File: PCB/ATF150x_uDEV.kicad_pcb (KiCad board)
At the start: 2 copper layers, 50.8 x 20.3 mm, 14 parts, among them J1 Altera JTAG-A+VPP, J2 VERT, J3 VERT, U1 ATF150x-xAx44

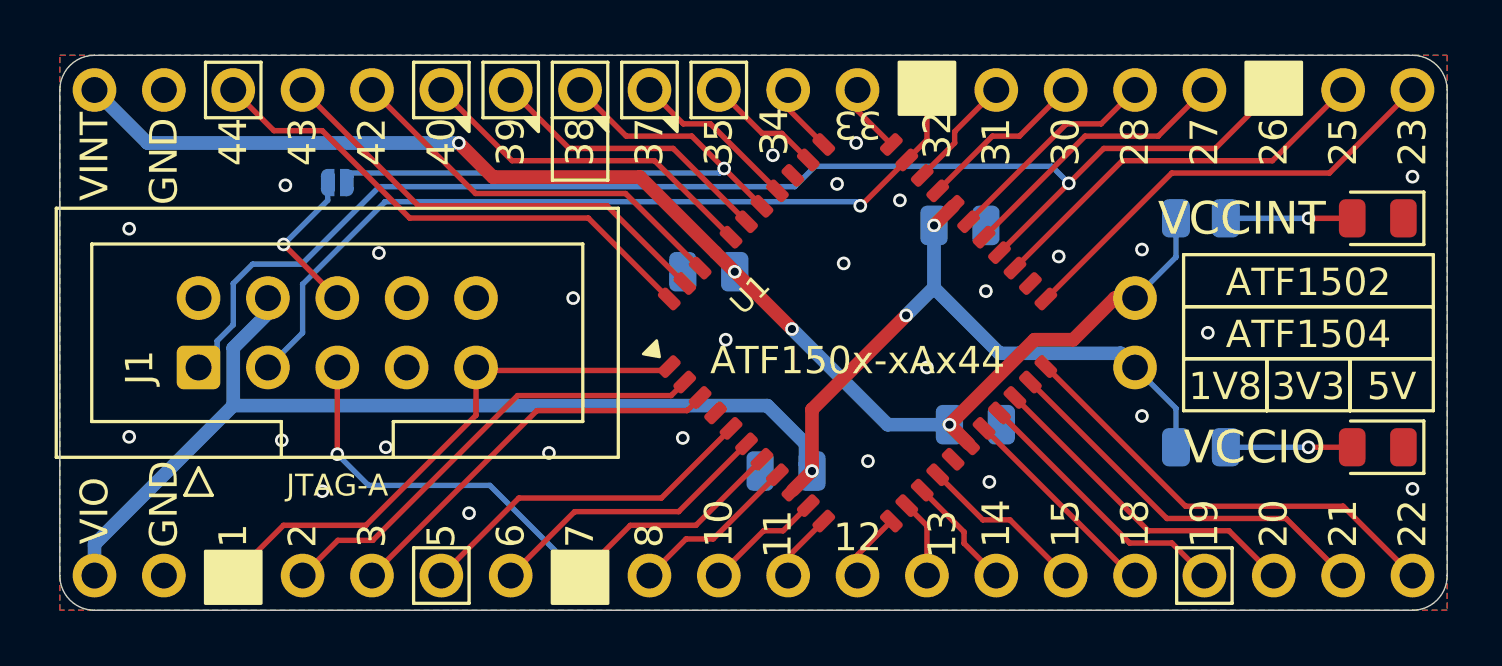
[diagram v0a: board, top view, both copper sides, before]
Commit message: correct pin 44 label, silkscreen, pics, move vpp jumper
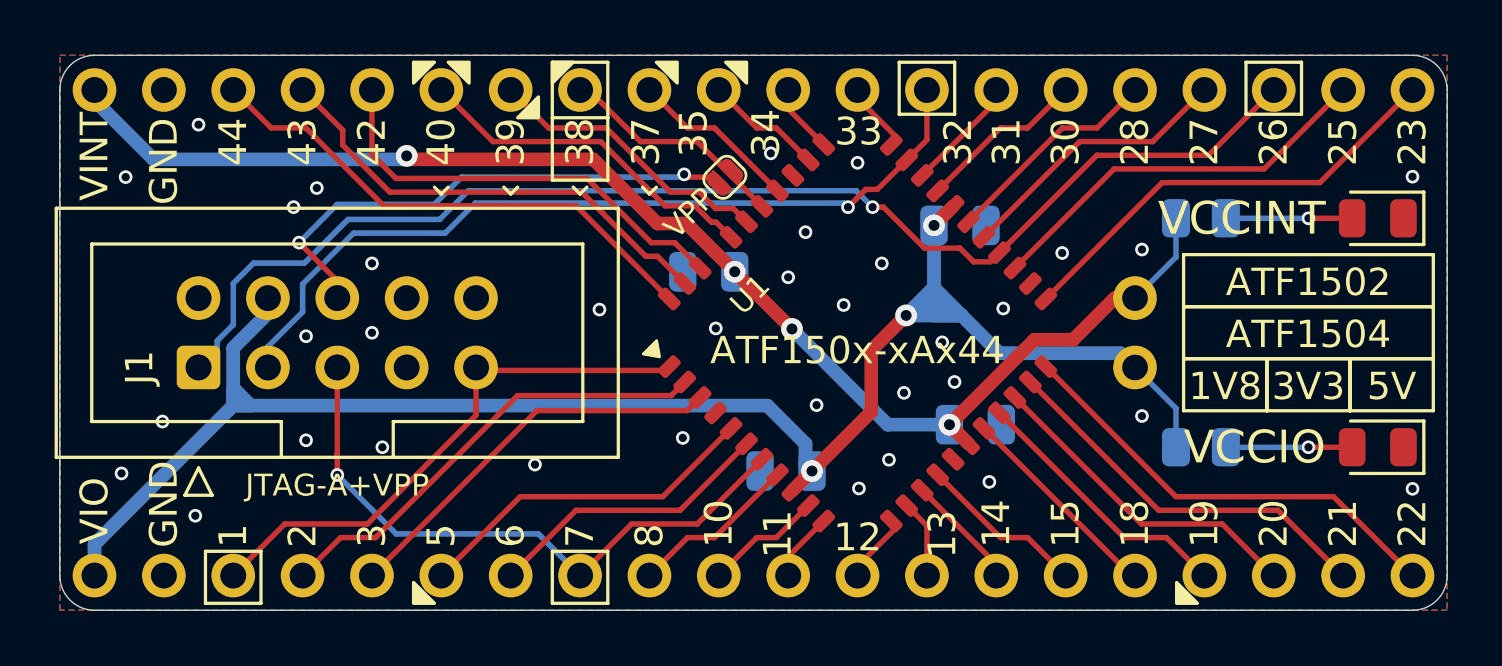
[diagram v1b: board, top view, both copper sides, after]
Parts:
- J2, J3: value VERT -> 1x20x2.54mm
- JP2: value DNP -> VPP; moved to F.Cu
- moved JP2 14.2 mm to (139.9, 94.6), turned to 45 degrees
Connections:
- net /44/PD1 renamed /44
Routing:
- net /38/OE1/Vpp: track 22.7 -> 8.54 mm, vias 1 -> 0
- net Net-(J1-VPP): track 5.71 -> 19.1 mm, vias 1 -> 2
- net VCCIO: track 60.4 -> 63.0 mm
- net /26/TCK: track 48.7 -> 46.8 mm
- net /42: track 14.7 -> 16.1 mm
- net GND: vias 27 -> 35
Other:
- board text added: "JTAG-A+VPP"
- board text added: "VCC"
- board text removed: "JTAG-A"
- board text removed: "VREF"

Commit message: pcb double vias on power traces
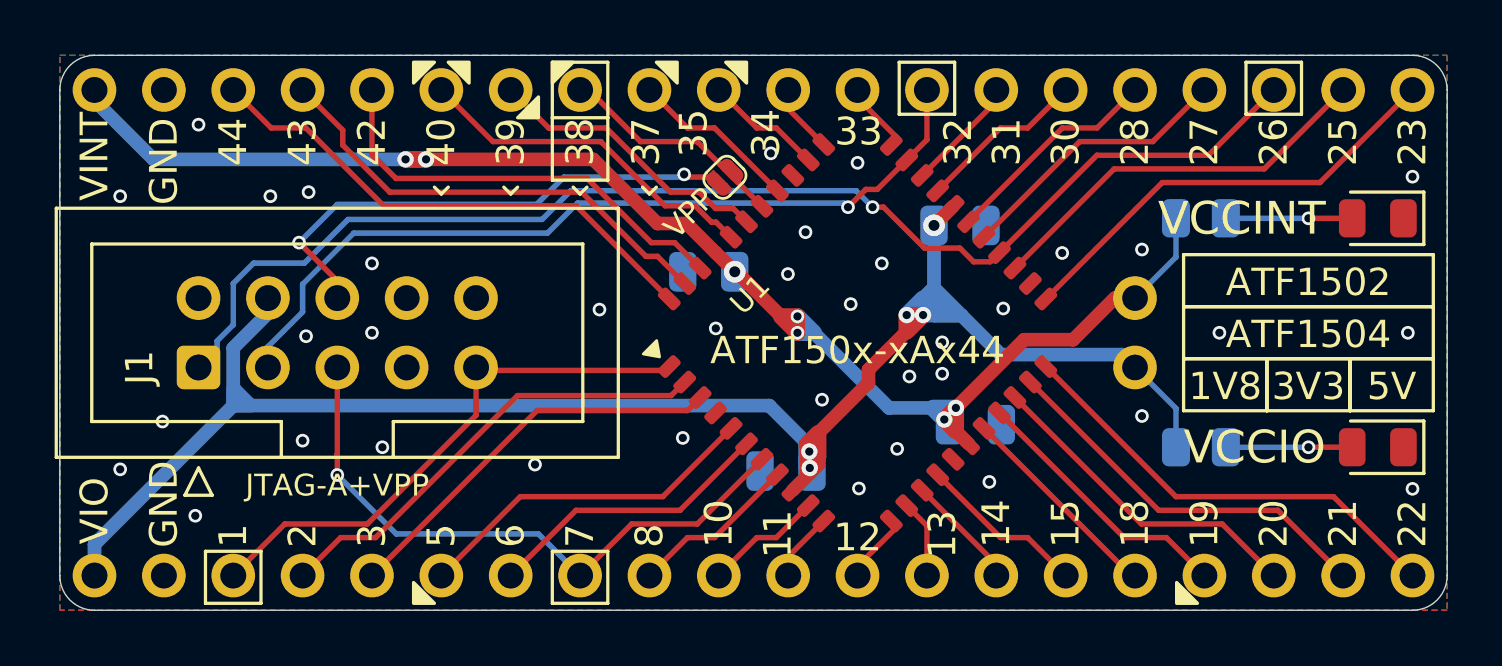
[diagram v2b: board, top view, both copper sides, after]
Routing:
- net VCCINT: track 50.0 -> 51.8 mm, vias 4 -> 7
- net VCCIO: track 63.0 -> 64.4 mm, vias 3 -> 5
- net GND: vias 35 -> 37
